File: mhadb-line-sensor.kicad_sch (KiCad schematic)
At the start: 32 parts, among them J1 Conn_01x04, J2 TC2030, J4 Conn_01x04_Pin, U1 STM32F103C8Tx, U3 SN65HVD230, Y1 8M

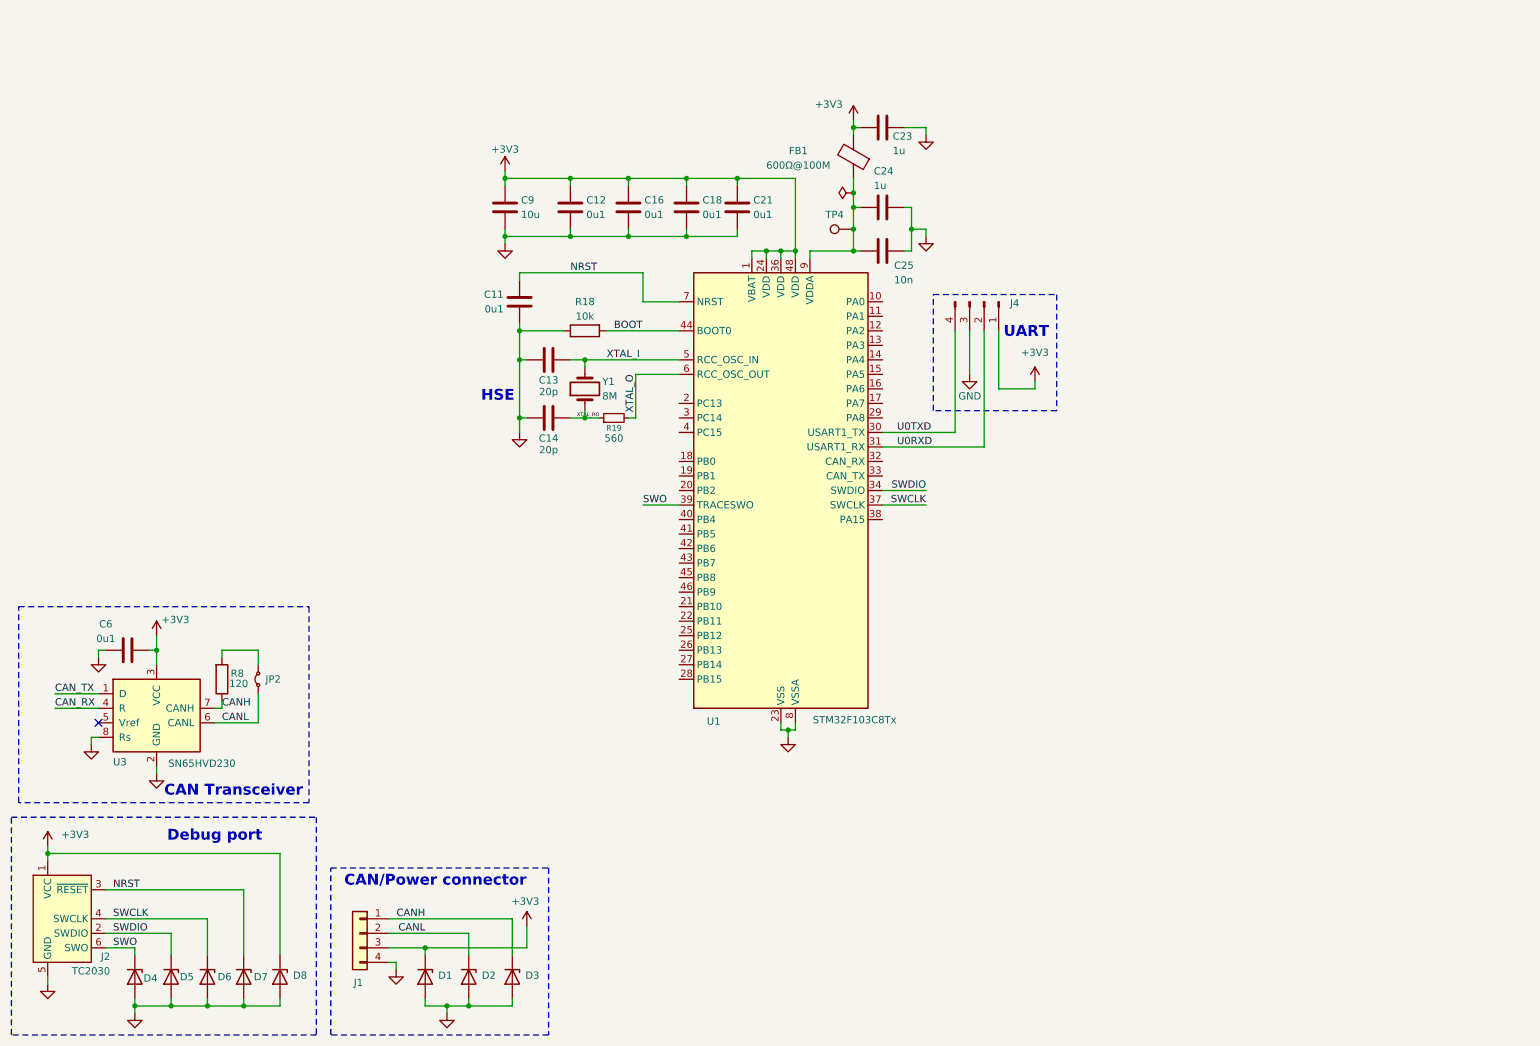
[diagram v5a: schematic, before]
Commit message: schem: add 10x QRE1113 reflective sensor
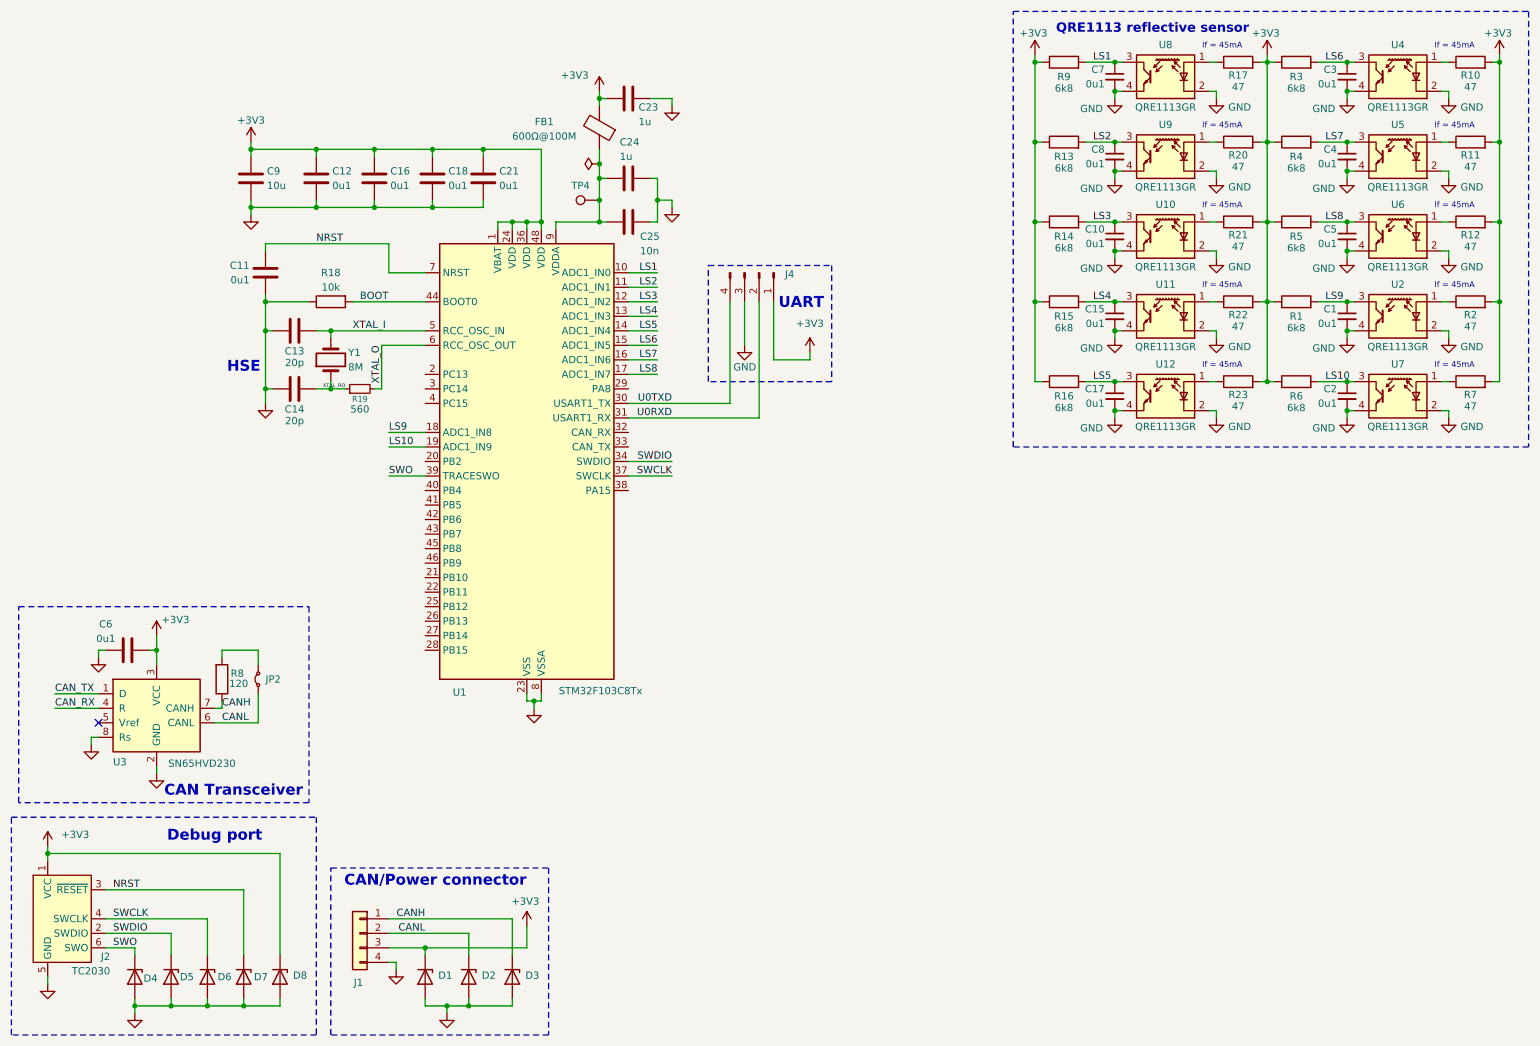
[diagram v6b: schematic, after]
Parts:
- added C1, C10, C15, C17, C2, C3, C4, C5, C7, C8: 0u1, Capacitor_SMD:C_0402_1005Metric, symbol Device:C_Small
- added R1, R13, R14, R15, R16, R3, R4, R5, R6, R9: 6k8, Resistor_SMD:R_0603_1608Metric, symbol Device:R
- added R10, R11, R12, R17, R2, R20, R21, R22, R23, R7: 47, Resistor_SMD:R_0603_1608Metric, symbol Device:R
- added U10, U11, U12, U2, U4, U5, U6, U7, U8, U9: QRE1113GR, OptoDevice:OnSemi_CASE100CY, symbol Sensor_Proximity:QRE1113GR
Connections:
- net +3V3: now also R1.1, R10.2, R11.2, R12.2, R13.1, R14.1, R15.1, R16.1, R17.2, R2.2, R20.2, R21.2, R22.2, R23.2, R3.1, R4.1, R5.1, R6.1, R7.2, R9.1
- net GND: now also C1.2, C10.2, C15.2, C17.2, C2.2, C3.2, C4.2, C5.2, C7.2, C8.2, U10.2 (K), U10.4, U11.2 (K), U11.4, U12.2 (K), U12.4, U2.2 (K), U2.4, U4.2 (K), U4.4, U5.2 (K), U5.4, U6.2 (K), U6.4, U7.2 (K), U7.4, U8.2 (K), U8.4, U9.2 (K), U9.4
- net LS1: now reaches U1.10 (PA0)
- net LS1: now also C7.1, R9.2, U8.3
- net LS2: now reaches U1.11 (PA1)
- net LS2: now also C8.1, R13.2, U9.3
- net LS3: now reaches U1.12 (PA2)
- net LS3: now also C10.1, R14.2, U10.3
- net LS4: now reaches U1.13 (PA3)
- net LS4: now also C15.1, R15.2, U11.3
- net LS5: now reaches U1.14 (PA4)
- net LS5: now also C17.1, R16.2, U12.3
- net LS6: now reaches U1.15 (PA5)
- net LS6: now also C3.1, R3.2, U4.3
- net LS7: now reaches U1.16 (PA6)
- net LS7: now also C4.1, R4.2, U5.3
- net LS8: now reaches U1.17 (PA7)
- net LS8: now also C5.1, R5.2, U6.3
- net LS9: now reaches U1.18 (PB0)
- net LS9: now also C1.1, R1.2, U2.3
- net LS10: now reaches U1.19 (PB1)
- net LS10: now also C2.1, R6.2, U7.3
- new net: R23.1, U12.1 (A)
- new net: R10.1, U4.1 (A)
- new net: R2.1, U2.1 (A)
- new net: R22.1, U11.1 (A)
- new net: R11.1, U5.1 (A)
- new net: R12.1, U6.1 (A)
- new net: R21.1, U10.1 (A)
- new net: R17.1, U8.1 (A)
- new net: R20.1, U9.1 (A)
- new net: R7.1, U7.1 (A)
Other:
- note added: "If = 45mA"
- note added: "QRE1113 reflective sensor"
- moved on the sheet: C11, C12, C13, C14, C16, C18, C21, C23, C24, C25, C9, FB1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

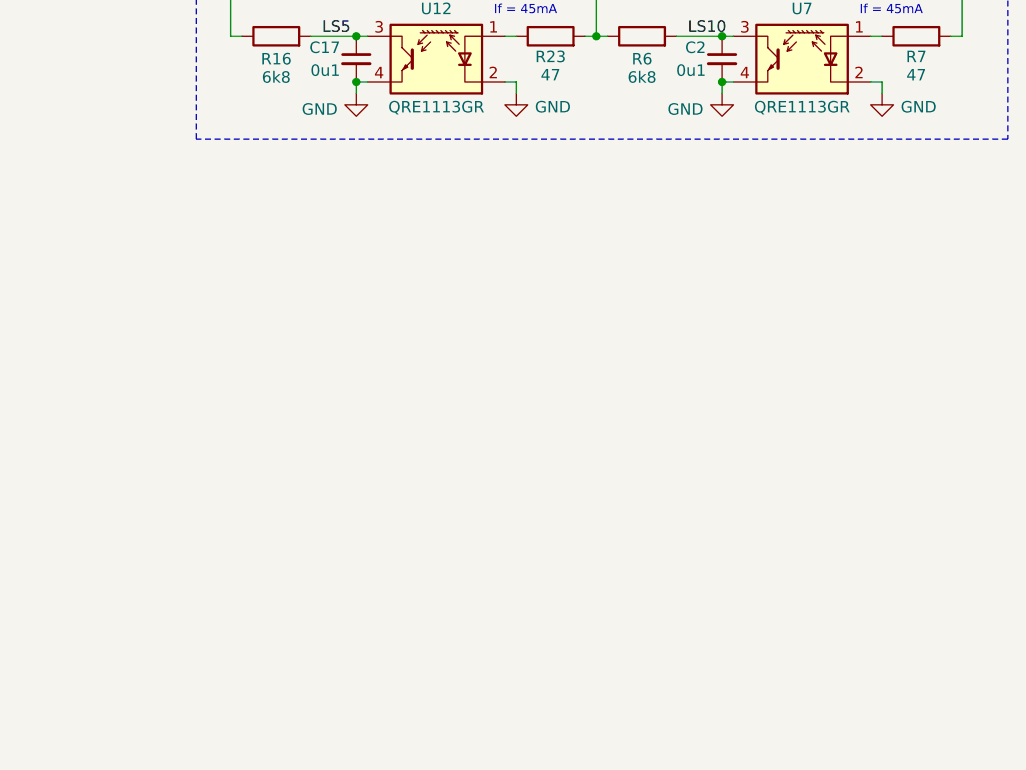
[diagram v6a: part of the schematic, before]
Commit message: schem: add 10x WS2812B RGB LEDs
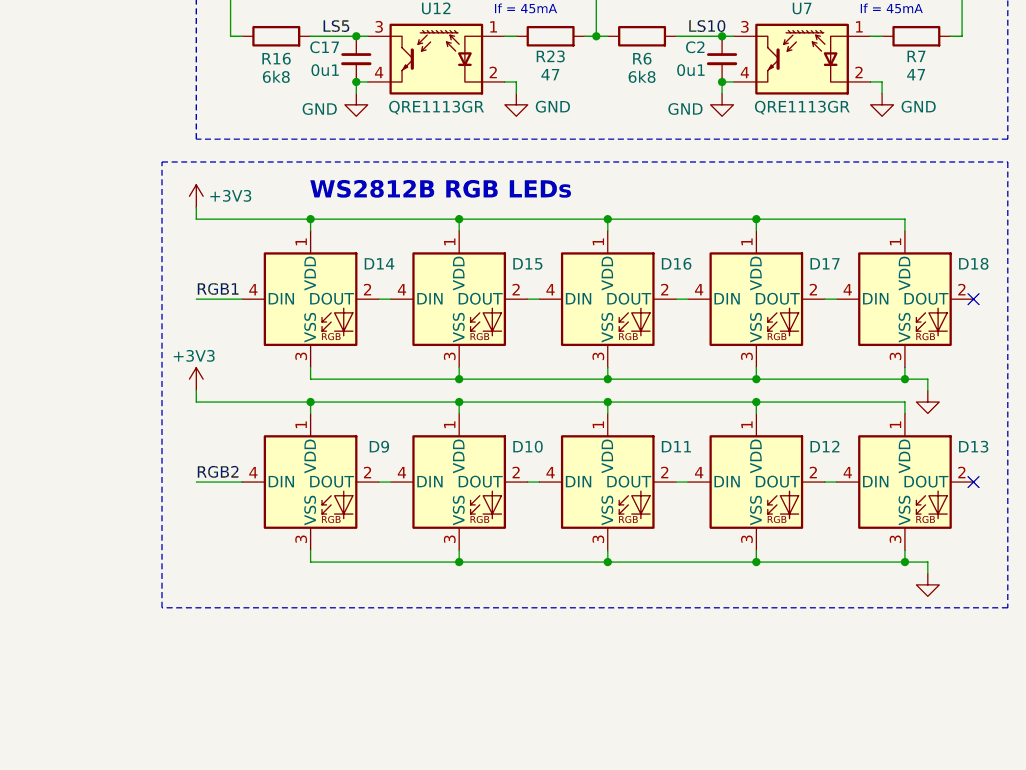
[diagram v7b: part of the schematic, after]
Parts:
- added D10, D11, D12, D13, D14, D15, D16, D17, D18, D9: WS2812B, LED_SMD:LED_WS2812B_PLCC4_5.0x5.0mm_P3.2mm, symbol LED:WS2812B
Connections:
- net +3V3: now also D10.1 (VDD), D11.1 (VDD), D12.1 (VDD), D13.1 (VDD), D14.1 (VDD), D15.1 (VDD), D16.1 (VDD), D17.1 (VDD), D18.1 (VDD), D9.1 (VDD)
- net GND: now also D10.3 (VSS), D11.3 (VSS), D12.3 (VSS), D13.3 (VSS), D14.3 (VSS), D15.3 (VSS), D16.3 (VSS), D17.3 (VSS), D18.3 (VSS), D9.3 (VSS)
- new net: D12.2 (DOUT), D13.4 (DIN)
- new net: D11.2 (DOUT), D12.4 (DIN)
- new net: D10.2 (DOUT), D11.4 (DIN)
- new net: D17.2 (DOUT), D18.4 (DIN)
- new net: D16.2 (DOUT), D17.4 (DIN)
- new net: D15.2 (DOUT), D16.4 (DIN)
- new net: D14.2 (DOUT), D15.4 (DIN)
- new net: D10.4 (DIN), D9.2 (DOUT)
- new net RGB1: D14.4 (DIN)
- new net RGB2: D9.4 (DIN)
- no-connect marks 1 -> 3
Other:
- note added: "WS2812B RGB LEDs"

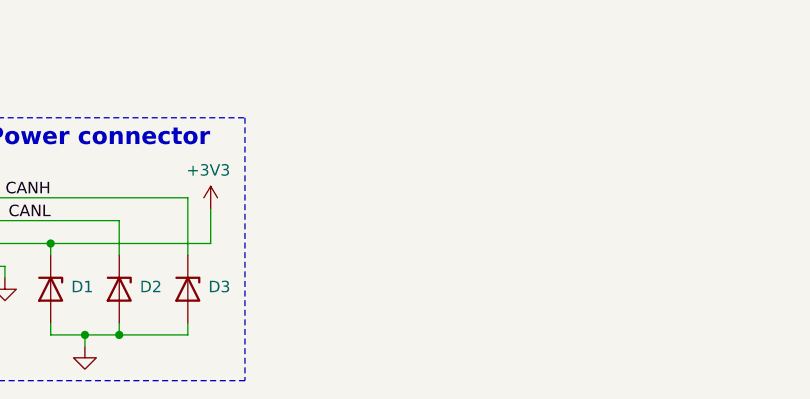
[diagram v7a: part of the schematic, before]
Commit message: schem: add BOOT and RST btns
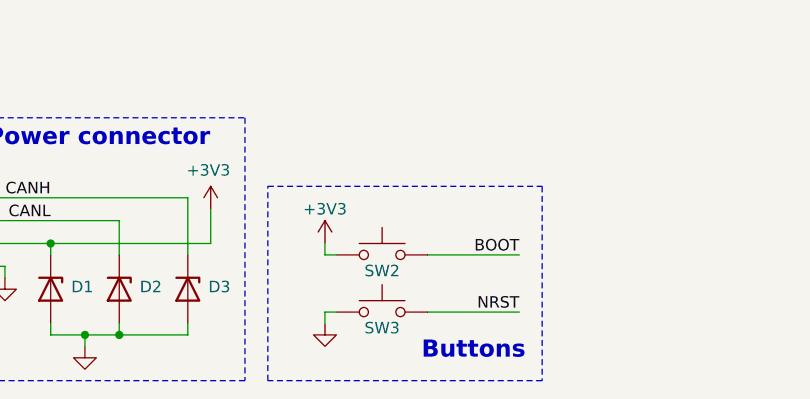
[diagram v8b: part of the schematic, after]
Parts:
- added SW2, SW3: SW_Push, Button_Switch_SMD:SW_SPST_TS-1088-xR020, symbol Switch:SW_Push
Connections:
- net +3V3: now also SW2.1
- net BOOT: now also SW2.2
- net GND: now also SW3.1
- net NRST: now also SW3.2
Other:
- note added: "Buttons"
